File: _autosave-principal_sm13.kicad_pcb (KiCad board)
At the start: 2 copper layers, 138.6 x 86.2 mm, 94 parts, among them J1 Conn_01x03, J2 Conn_01x03, J3 Conn_01x03, J4 Conn_01x03, J5 Conn_01x03, J6 Conn_01x03, J7 Conn_01x03, J8 Conn_01x03, P12 CONN_10X2, P14 SPI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

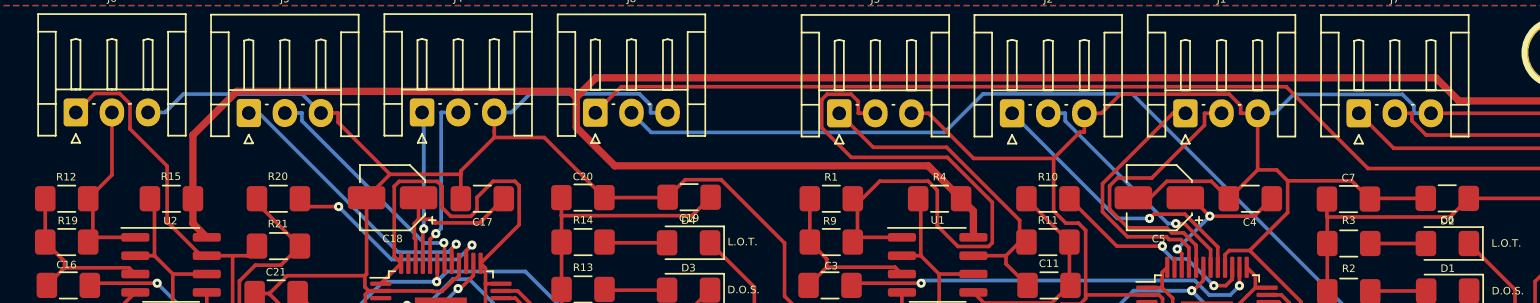
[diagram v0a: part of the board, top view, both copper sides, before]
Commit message: cambiados conectores, agregado conversor 3,3->TTL drivers
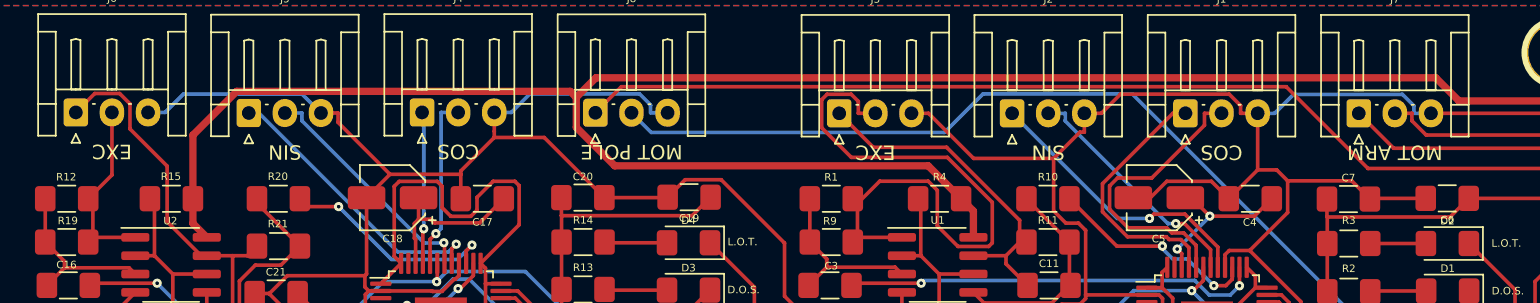
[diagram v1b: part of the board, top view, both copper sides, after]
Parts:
- J1, J4: value Conn_01x03 -> COS
- J2, J5: value Conn_01x03 -> SIN
- J3, J6: value Conn_01x03 -> EXC
- J7: value Conn_01x03 -> MOT ARM
- J8: value Conn_01x03 -> MOT POLE
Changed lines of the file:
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@@
       (effects (font (size 0.52 0.52) (thickness 0.12)))
     )
-    (fp_text value Conn_01x03 (at 2.5 2.7) (layer F.Fab)
+    (fp_text value "MOT POLE" (at 2.5 2.7 180 unlocked) (layer F.SilkS)
       (effects (font (size 1 1) (thickness 0.15)))
     )
@@
       (effects (font (size 0.52 0.52) (thickness 0.12)))
     )
-    (fp_text value Conn_01x03 (at 2.5 2.7) (layer F.Fab)
+    (fp_text value "MOT ARM" (at 2.5 2.7 180 unlocked) (layer F.SilkS)
       (effects (font (size 1 1) (thickness 0.15)))
     )
@@
       (effects (font (size 0.52 0.52) (thickness 0.12)))
     )
-    (fp_text value Conn_01x03 (at 2.5 2.7) (layer F.Fab)
+    (fp_text value EXC (at 2.5 2.7 180 unlocked) (layer F.SilkS)
       (effects (font (size 1 1) (thickness 0.15)))
     )
@@
       (effects (font (size 0.52 0.52) (thickness 0.12)))
     )
-    (fp_text value Conn_01x03 (at 2.5 2.7) (layer F.Fab)
+    (fp_text value SIN (at 2.5 2.7 180 unlocked) (layer F.SilkS)
       (effects (font (size 1 1) (thickness 0.15)))
     )
@@
       (effects (font (size 0.52 0.52) (thickness 0.12)))
     )
-    (fp_text value Conn_01x03 (at 2.5 2.7) (layer F.Fab)
+    (fp_text value COS (at 2.5 2.7 180 unlocked) (layer F.SilkS)
       (effects (font (size 1 1) (thickness 0.15)))
     )
@@
       (effects (font (size 0.52 0.52) (thickness 0.12)))
     )
-    (fp_text value Conn_01x03 (at 2.5 2.7) (layer F.Fab)
+    (fp_text value EXC (at 2.5 2.7 180 unlocked) (layer F.SilkS)
       (effects (font (size 1 1) (thickness 0.15)))
     )
@@
       (effects (font (size 0.52 0.52) (thickness 0.12)))
     )
-    (fp_text value Conn_01x03 (at 2.5 2.7) (layer F.Fab)
+    (fp_text value SIN (at 2.5 2.7 180 unlocked) (layer F.SilkS)
       (effects (font (size 1 1) (thickness 0.15)))
     )
@@
       (effects (font (size 0.52 0.52) (thickness 0.12)))
     )
-    (fp_text value Conn_01x03 (at 2.5 2.7) (layer F.Fab)
-      (effects (font (size 1 1) (thickness 0.15)))
-    )
+    (fp_text value COS (at 2.5 2.7 180 unlocked) (layer F.SilkS)
+      (effects (font (size 1 1) (thickness 0.15)))
+    )
